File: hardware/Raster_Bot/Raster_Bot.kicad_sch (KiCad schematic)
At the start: 65 parts, among them J1 JST_PH, J2 USB_C_Receptacle_USB2.0_16P, J3 Conn_EYESPI, J4 Conn_Motor_N20_Encoder, J6 Conn_Motor_N20_Encoder, Q1 AO3401A, Q2 AO3401A, Q3 2N7002, SW1 SW_SPDT_SH, SW2 SW_RESET, SW3 SW_BOOT, U1 AP2114H-3.3, U2 BQ24072RGT, U3 ESP32-S3-MINI-1, U4 TPS61023DRLR, U5 DRV8833PWPR

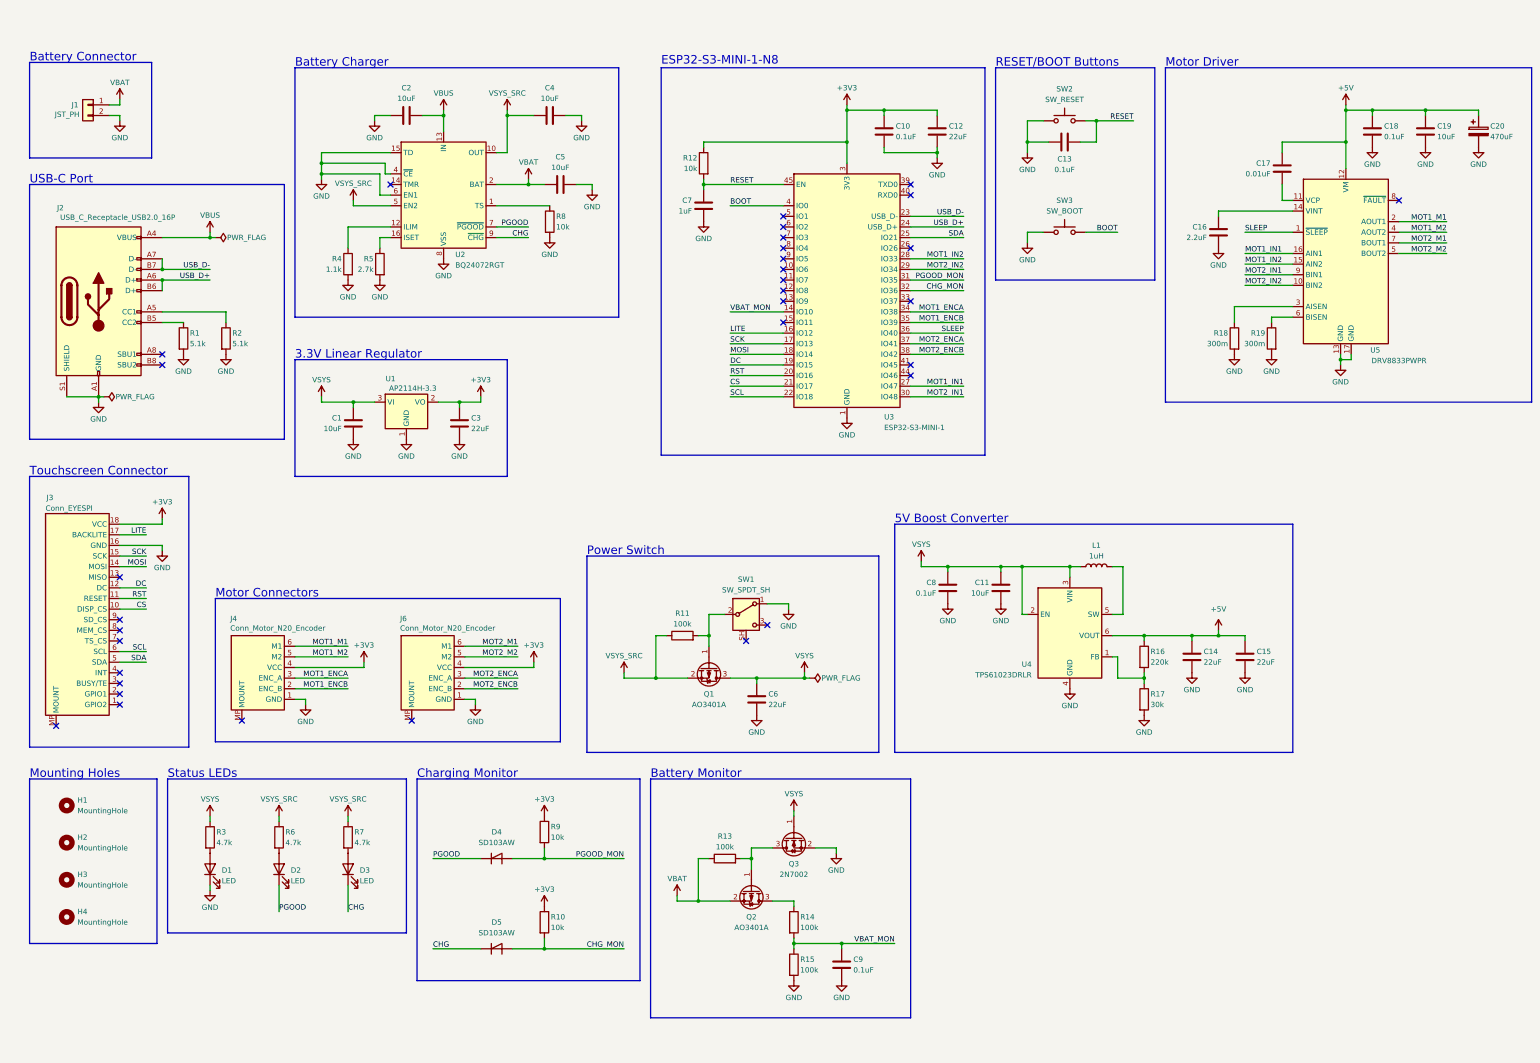
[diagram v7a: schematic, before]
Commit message: [hardware] v0.6 - Add silkscreen logo; Reposition footprints; Remove custom USB footprint
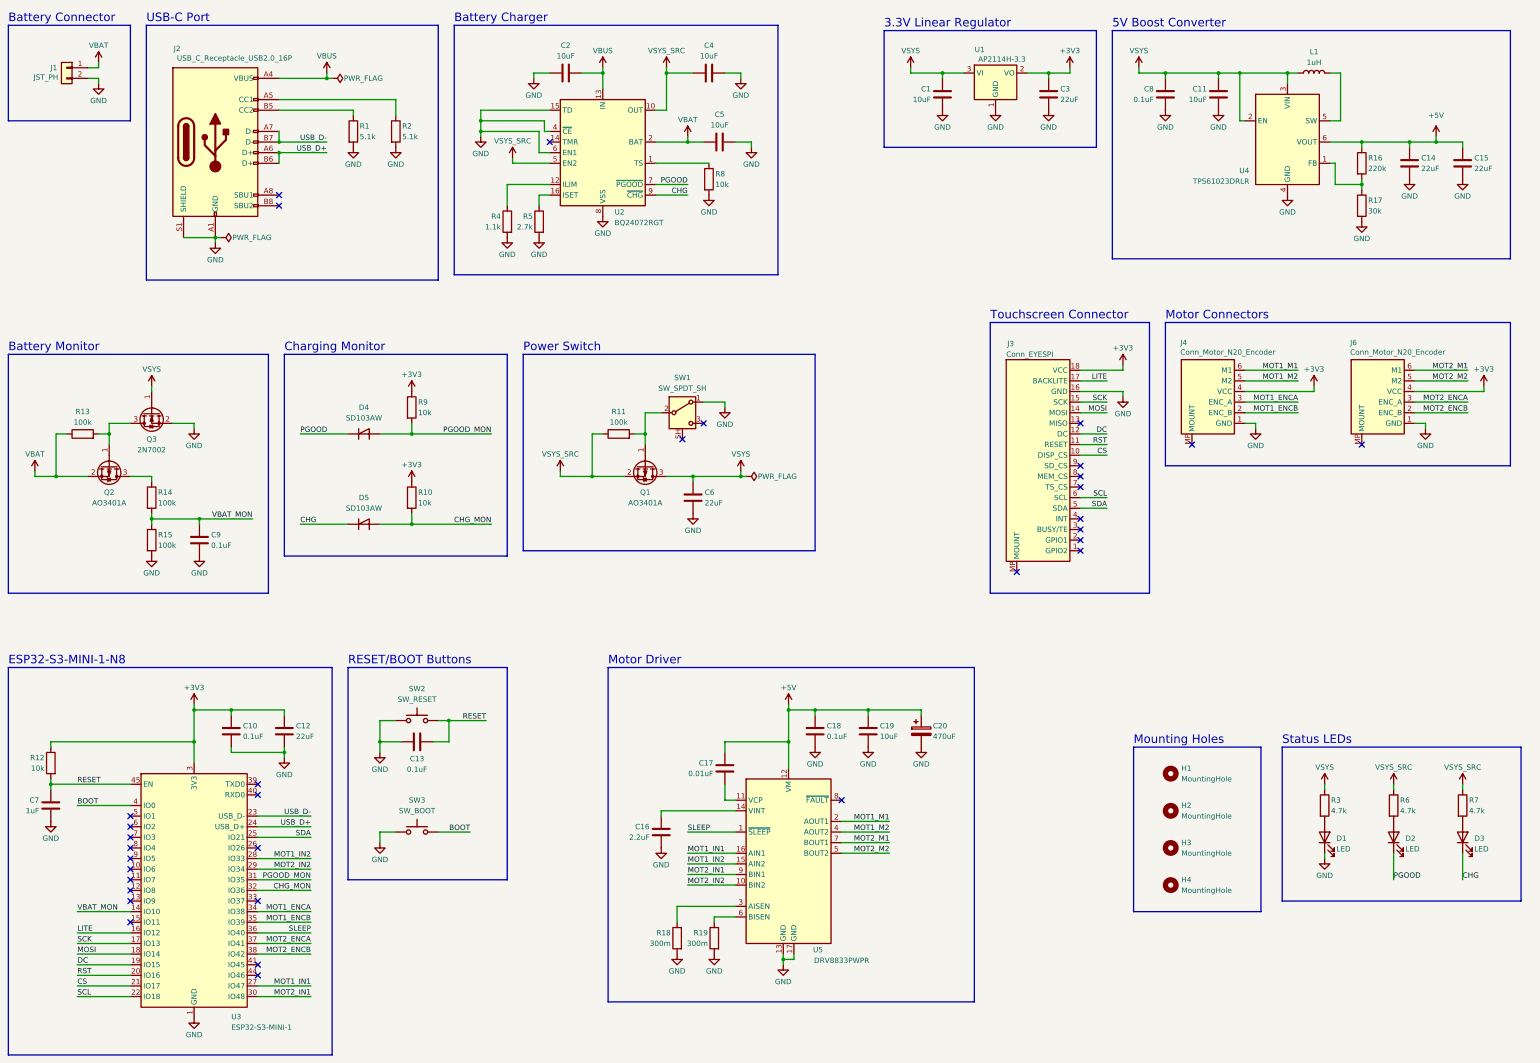
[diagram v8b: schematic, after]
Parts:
- J2: symbol Raster_Bot:USB_C_Receptacle_USB2.0_16P -> Connector:USB_C_Receptacle_USB2.0_16P
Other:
- moved on the sheet: C1, C10, C11, C12, C13, C14, C15, C16, C17, C18, C19, C2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
